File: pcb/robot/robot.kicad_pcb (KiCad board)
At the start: 4 copper layers, 80 x 70 mm, 381 parts, among them IC1 TPS22998RYZR, J1 USB4151-GF-C, J3 USBC_Receptacle_SMD_RA, J4 Conn_01x02, J6 Conn_01x06_MountingPin, J7 Conn_01x06_MountingPin, J9 Conn_01x05, Q1 Q_NMOS_GDS, Q2 AS2312, Q3 YJL3416A, Q4 Q_NMOS_GDS, Q5 EFC8811R-TF, Q6 SN74AHC125RGYR, SW1 SW_SPST, U1 AP2502KTR-G1, U10 TPD1E05U06, U11 MAX77958EWV+T, U12 TPS22950CDDCR, U13 TPS61253AYFFT, U14 NCP3901, U15 TPD1E05U06, U16 TVS0500DRV, U17 TPD1E05U06, U18 TPD1E05U06, U19 TPD1E05U06, U2 TPS63021DSJR, U20 AP33771DKZ-13, U21 LSF0102DCTR, U22 BQ27742YZFR-G1, U23 MAX77857BEWB+, U24 W25Q128JVS, U25 DRV8830DRCR, U26 DRV8830DRCR, U27 STWLC38JRM, U28 MAX77976EFD+, U29 RP2040, U3 XC6206PxxxMR, U30 TPS3808G01DBVR, U31 TPS3808G01DBVR, U4 TPD1E05U06, U5 TPD1E05U06, U6 TVS0500DRV, U7 TPD1E05U06, U8 TPD1E05U06, U9 TPD1E05U06, Y1 ECS-120-8-36-CKM-TR3

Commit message: Move S2 back to its original position (fixes #20)
S2 (the USB data switch, JS202011JCQN) ended up on the wrong side of
the board when the USB-PD module got merged back in - fine
electrically, but the 3D-printed bodies have the access hole cut for
where it used to sit, so it would've been covered by the case.

Moved it back, along with TP19/TP20 since those are the test points
sitting right on its switched USB lines (DIFF_SWITCHED_N/P) - no
reason to leave them stranded away from what they're probing.

Checked against the original pre-split design: S2 lands back on the
exact same coordinates it had there. Nets are unchanged on all three
parts, 0 unconnected items, no new DRC issues around this area.
Bumped the differential-pair via size back up to 0.5/0.2 while
rerouting the diff pair into its new spot.
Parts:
- moved TP19 61.3 mm to (138.0, 96.2), turned to 180 degrees
- moved TP20 60.7 mm to (135.7, 96.2), turned to 180 degrees
- moved S2 48.9 mm to (136.8, 102.2), turned to 90 degrees
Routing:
- net /USB-PD-PhonePC/DIFF_SWITCHED_N: track 38.1 -> 92.9 mm, vias 0 -> 2
- net /USB-PD-PhonePC/DIFF_SWITCHED_P: track 37.4 -> 90.6 mm, vias 0 -> 2
- net /USB-PD-PhonePC/DIFF_EXT_P: track 54.2 -> 104.4 mm
- net /DP1: track 55.4 -> 5.52 mm
- net /USB-PD-PhonePC/DIFF_EXT_N: track 59.0 -> 106.0 mm
- net /DN1: track 51.9 -> 5.48 mm
- net GND: vias 198 -> 194

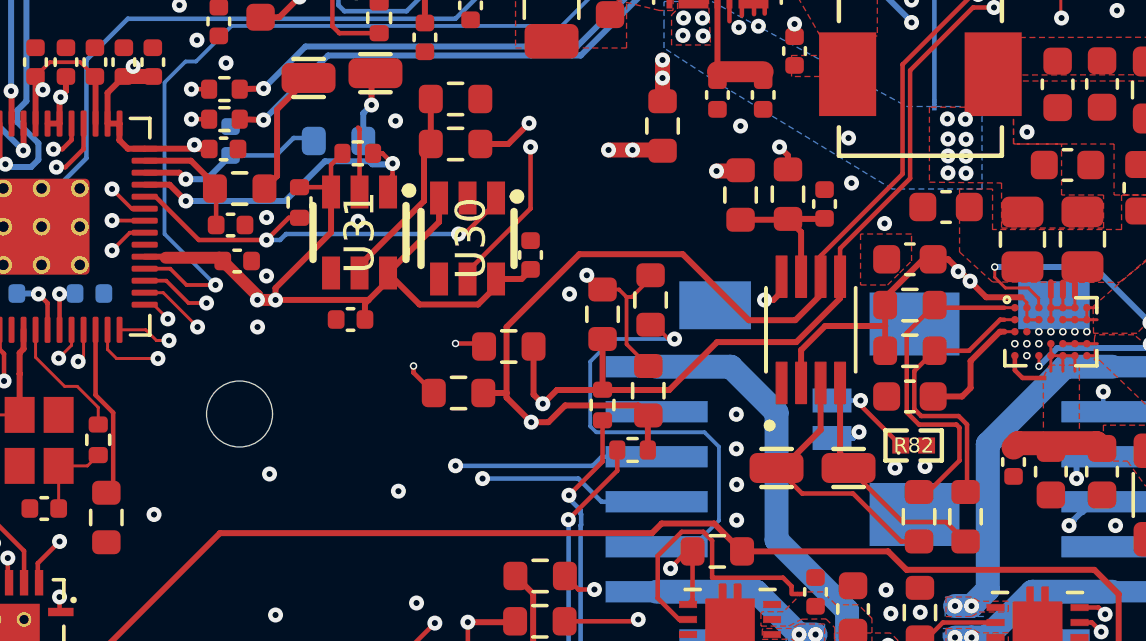
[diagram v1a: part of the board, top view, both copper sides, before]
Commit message: Remove leftover Conn_01x16, tidy up hierarchical labels (fixes #21)
Deleted J2, the old castellated-edge connector placeholder left over from when USB-PD was a separate board - it's been DNP/off-board since the reunification and wasn't even in the netlist, so nothing to reroute. Reconnected the signals that used to fan into it (USB_Phone_SYS, PGND, VCIN, SCL_M/SDA_M, INTB_SL, AGND, VIO1/VIO2, SCL_SL/SDA_SL, DP1/DN1) with proper hierarchical labels instead. Checked ERC/DRC before and after: same connectivity, 0 unconnected items, no new violations - the only thing that dropped off was the "footprint not in library" warning J2 itself used to trigger.
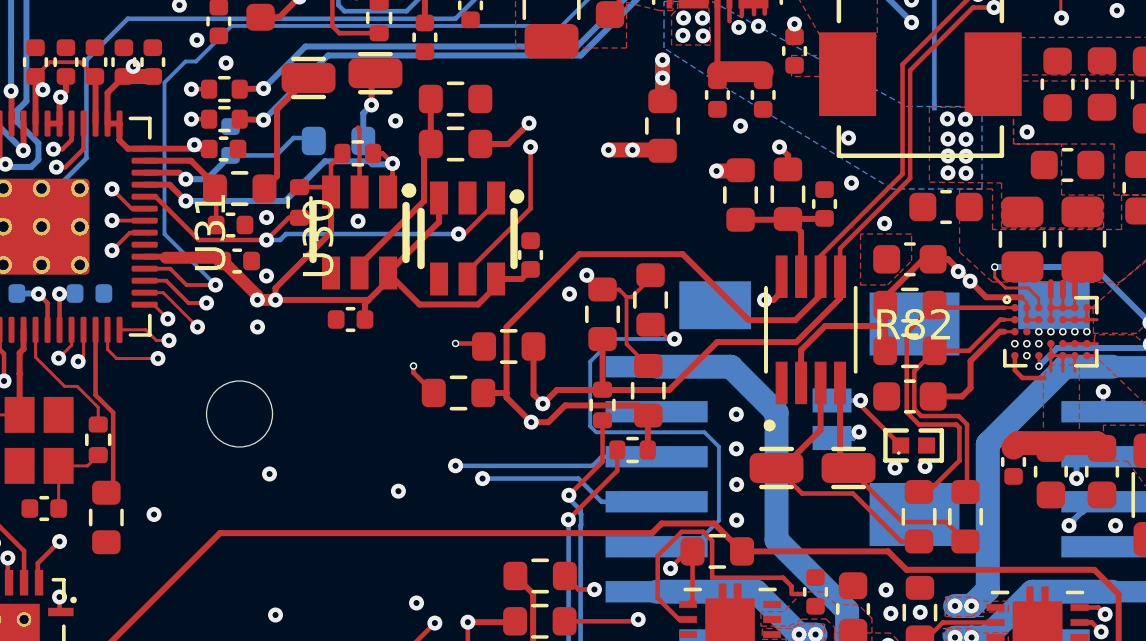
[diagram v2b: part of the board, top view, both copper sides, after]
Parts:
- R82: footprint robot:R0402 -> easyeda2kicad:R0402
- U3: footprint robot:SOT-23-3 -> Package_TO_SOT_SMD:SOT-23-3
- U30, U31: footprint robot:SOT-23-6_L2.9-W1.6-P0.95-LS2.8-BR -> easyeda2kicad:SOT-23-6_L2.9-W1.6-P0.95-LS2.8-BR
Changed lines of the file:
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@@
 		)
 	)
-	(footprint "robot:R0402"
+	(footprint "easyeda2kicad:R0402"
 		(layer "F.Cu")
 		(at 100.97 131.05)
 		(descr "100Ω (1000) ±1%")
 		(property "Reference" "R82"
-			(at 0 0 0)
+			(at 0 -4 0)
 			(layer "F.SilkS")
 			(effects
 				(font
-					(size 0.5 0.5)
-					(thickness 0.125)
+					(size 1 1)
+					(thickness 0.15)
 				)
 			)
@@
 			(at 0 4 0)
 			(layer "F.Fab")
-			(hide yes)
 			(effects
 				(font
@@
 			(layer "F.CrtYd")
 		)
+		(fp_text user "${REFERENCE}"
+			(at 0 0 0)
+			(layer "F.Fab")
+			(effects
+				(font
+					(size 1 1)
+					(thickness 0.15)
+				)
+			)
+		)
 		(pad "1" smd rect
 			(at -0.43 0)
@@
 		(fp_text user "*"
 			(at -1.4732 -2.6518 0)
+			(unlocked yes)
 			(layer "F.SilkS")
 			(effects
@@
 		(fp_text user "*"
 			(at -1.4732 -2.6518 0)
-			(unlocked yes)
 			(layer "F.SilkS")
 			(effects
@@
 		)
 	)
-	(footprint "robot:SOT-23-3"
+	(footprint "Package_TO_SOT_SMD:SOT-23-3"
 		(layer "F.Cu")
 		(at 133.59 115.3025 -90)
@@
 		(tags "SOT TO_SOT_SMD")
 		(property "Reference" "U3"
-			(at 0 -2.4 90)
+			(at 0 -2.4 270)
 			(layer "F.SilkS")
 			(effects
@@
 		)
 		(property "Value" "XC6206PxxxMR"
-			(at 0 2.4 90)
+			(at 0 2.4 270)
 			(layer "F.Fab")
-			(hide yes)
 			(effects
 				(font
@@
 		)
 		(property "Datasheet" "https://www.torexsemi.com/file/xc6206/XC6206.pdf"
-			(at 0 0 90)
+			(at 0 0 270)
 			(layer "F.Fab")
 			(hide yes)
@@
 		)
 		(property "Description" "Positive 60-250mA Low Dropout Regulator, Fixed Output, SOT-23"
-			(at 0 0 90)
+			(at 0 0 270)
 			(layer "F.Fab")
 			(hide yes)
@@
 		)
 	)
-	(footprint "robot:SOT-23-6_L2.9-W1.6-P0.95-LS2.8-BR"
+	(footprint "easyeda2kicad:SOT-23-6_L2.9-W1.6-P0.95-LS2.8-BR"
 		(layer "F.Cu")
 		(at 82.5 123.95 90)
 		(property "Reference" "U31"
-			(at 0 0 90)
+			(at 0 -4.95 90)
 			(layer "F.SilkS")
 			(effects
@@
 			(at 0 4.95 90)
 			(layer "F.Fab")
-			(hide yes)
 			(effects
 				(font
@@
 			)
 		)
-		(property "MPN" "TPS3808G01DBVR"
-			(at 0 0 90)
-			(unlocked yes)
-			(layer "F.Fab")
-			(hide yes)
-			(effects
-				(font
-					(size 1 1)
-					(thickness 0.15)
-				)
-			)
-		)
 		(property "Part Number" "TPS3808G01DBVR"
 			(at 0 0 90)
@@
 		)
 	)
-	(footprint "robot:SOT-23-6_L2.9-W1.6-P0.95-LS2.8-BR"
+	(footprint "easyeda2kicad:SOT-23-6_L2.9-W1.6-P0.95-LS2.8-BR"
 		(layer "F.Cu")
 		(at 86.1 124.15 90)
 		(property "Reference" "U30"
-			(at 0 0.11 90)
+			(at 0 -4.95 90)
 			(layer "F.SilkS")
 			(effects
@@
 			(at 0 4.95 90)
 			(layer "F.Fab")
-			(hide yes)
 			(effects
 				(font
@@
 			(at 0 0 90)
 			(unlocked yes)
-			(layer "F.Fab")
-			(hide yes)
-			(effects
-				(font
-					(size 1 1)
-					(thickness 0.15)
-				)
-			)
-		)
-		(property "MPN" "TPS3808G01DBVR"
-			(at 0 0 90)
-			(unlocked yes)
